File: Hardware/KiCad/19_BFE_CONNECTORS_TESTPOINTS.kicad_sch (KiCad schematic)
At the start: 0 parts

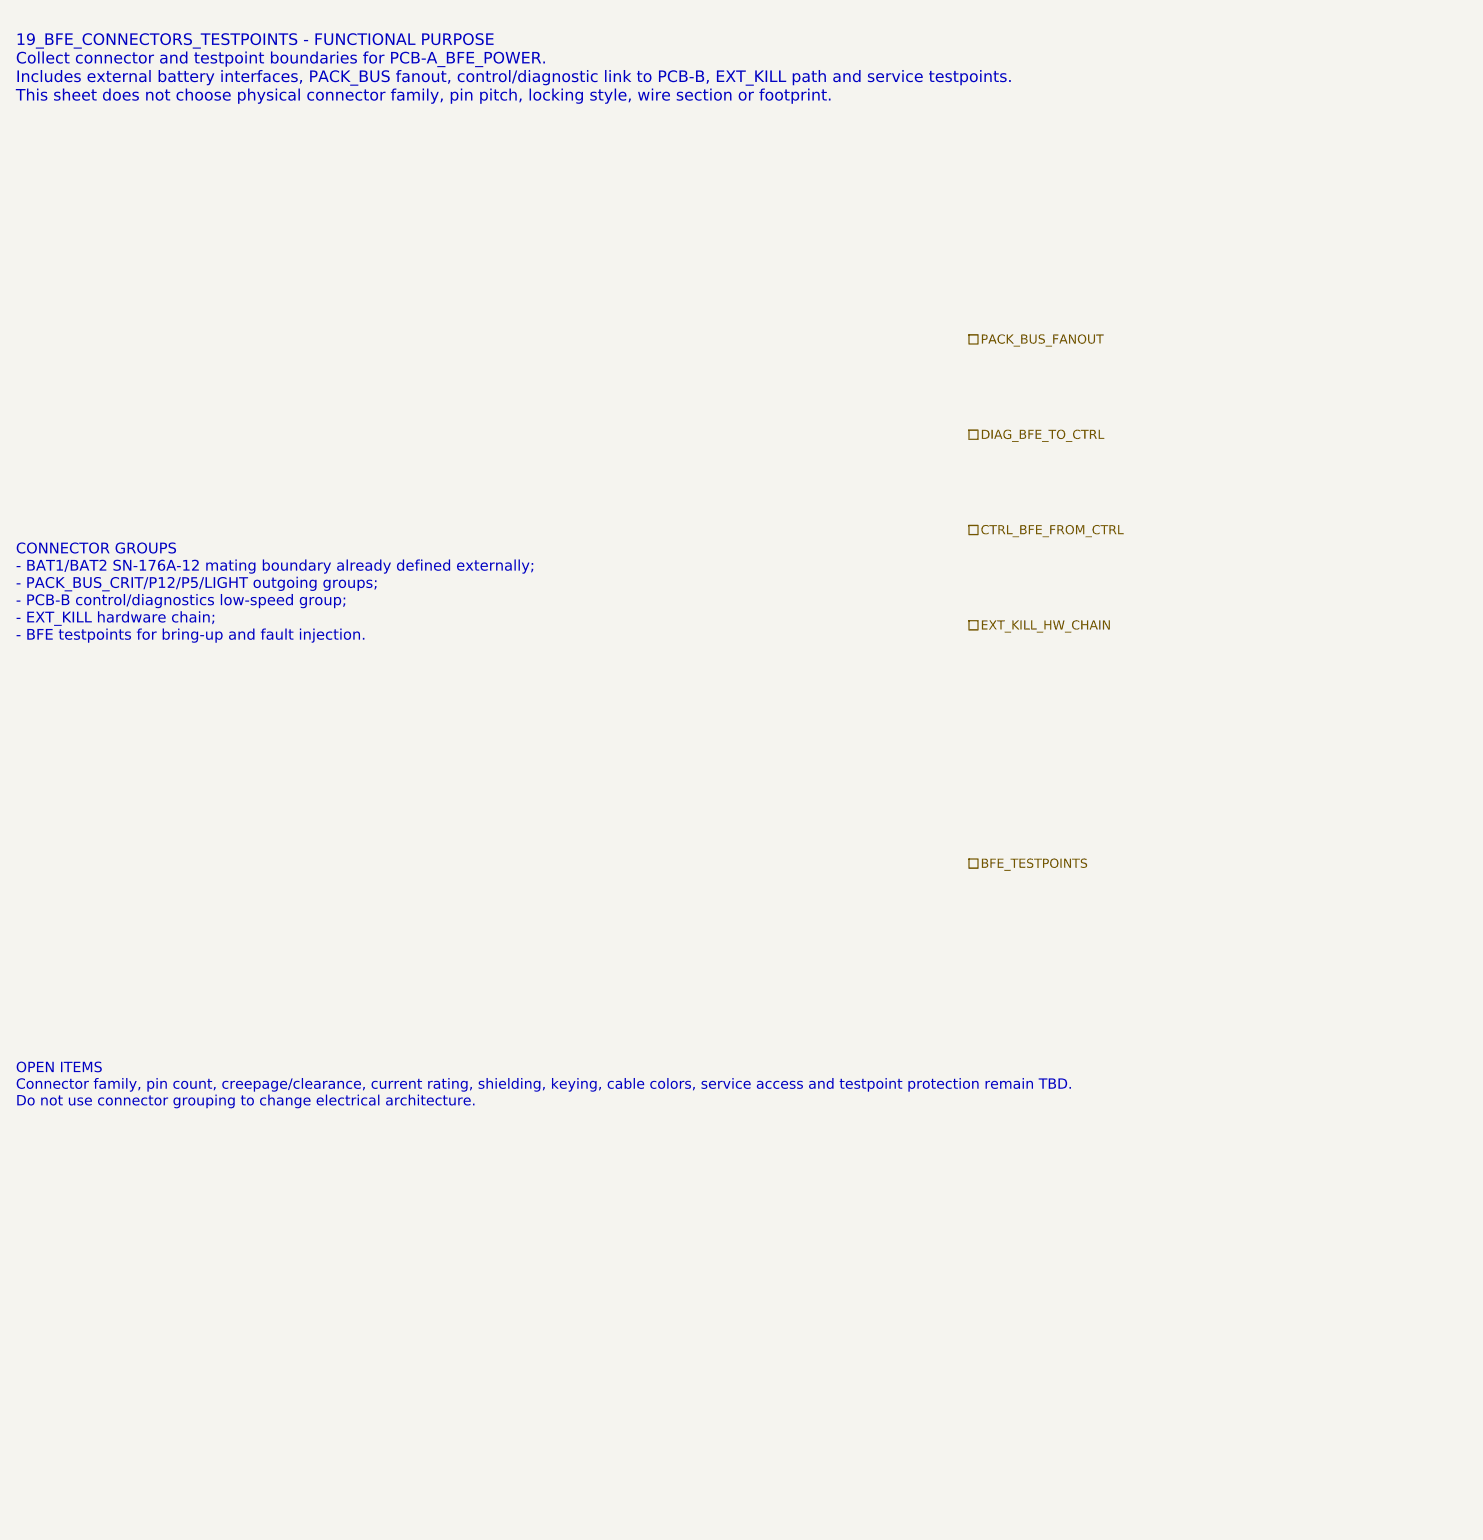
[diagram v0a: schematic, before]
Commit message: hardware: refine BFE connectors and testpoints level B
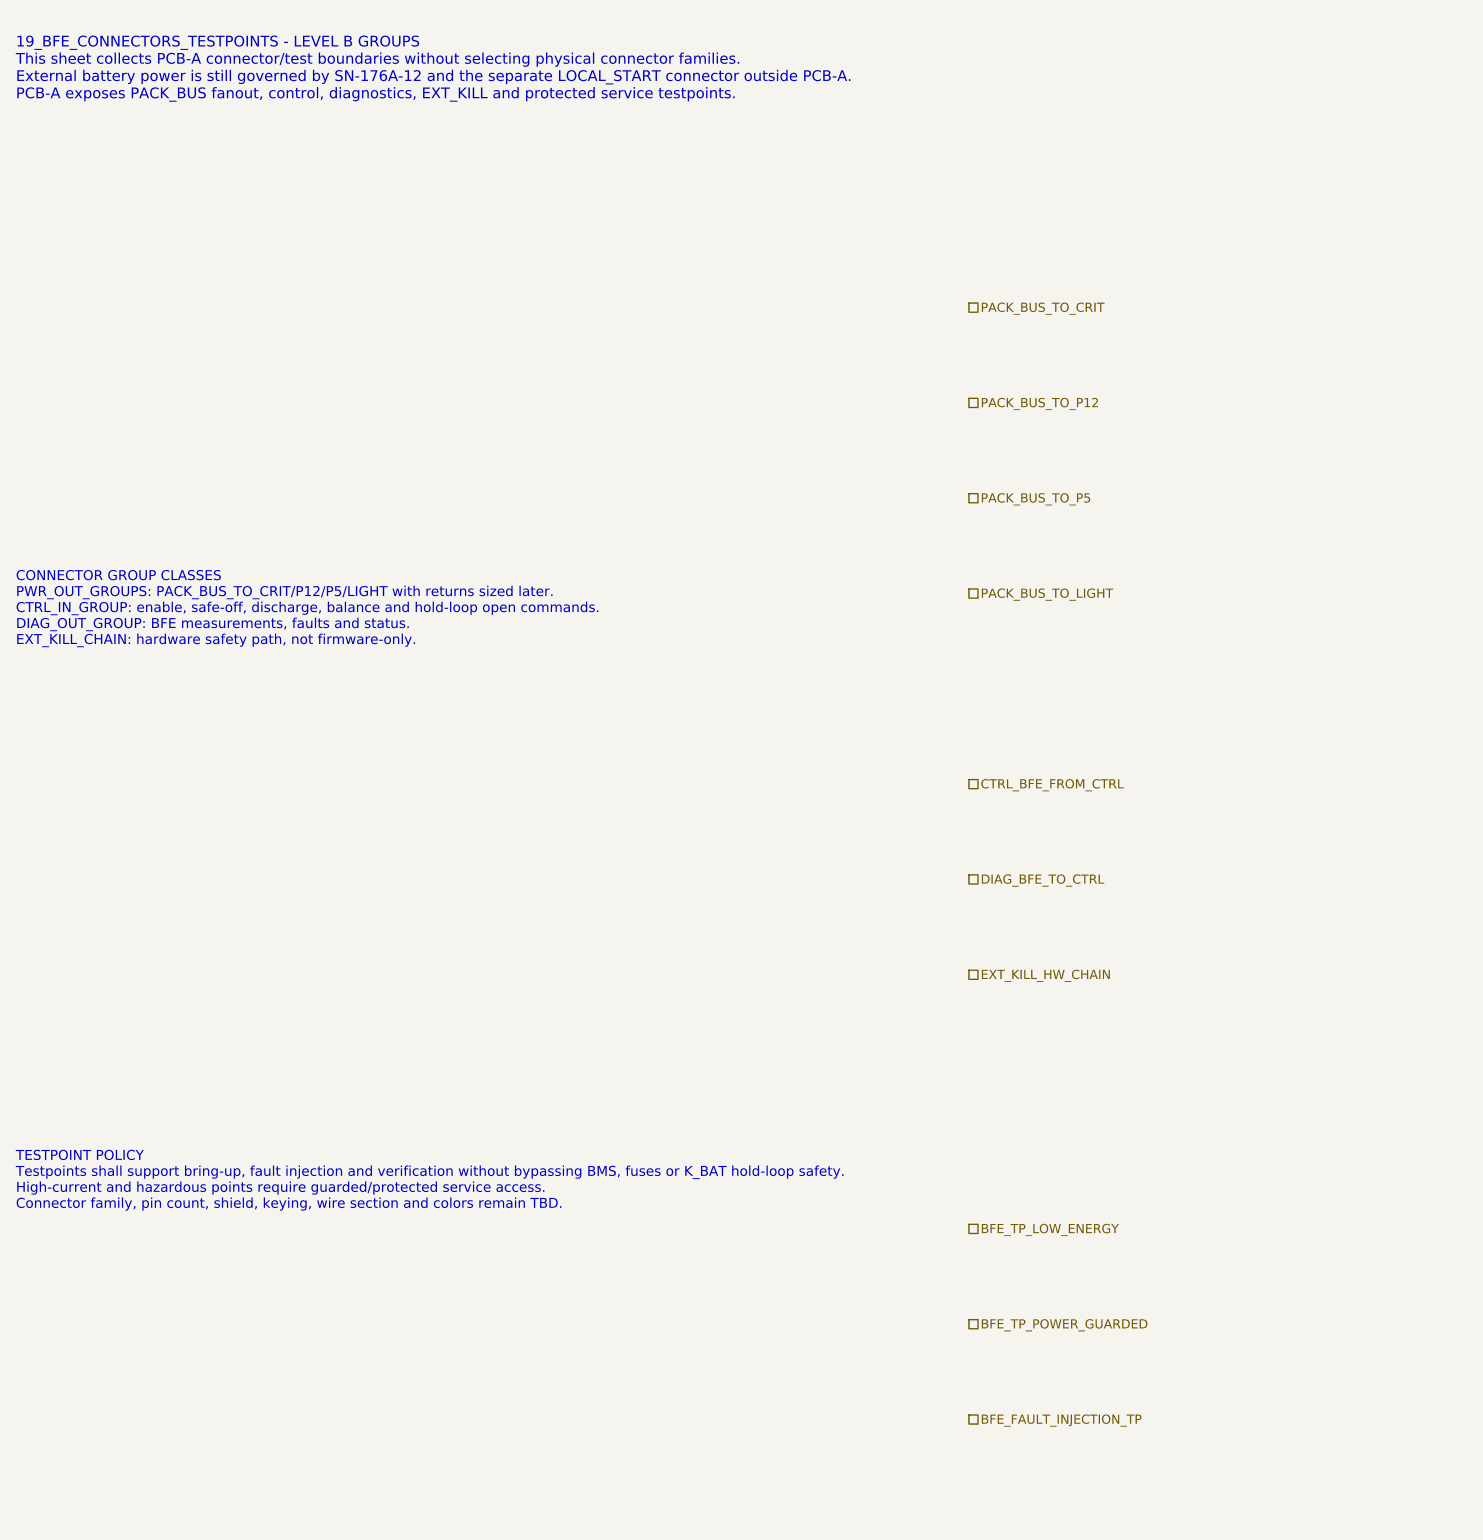
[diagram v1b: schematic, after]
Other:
- note added: "19_BFE_CONNECTORS_TESTPOINTS - LEVEL B GROUPS This sheet collects PCB-A connector/test boundaries without selecting physical connector families. External battery power is still governed by SN-176A-12 and the separate LOCAL_START connector outside PCB-A. PCB-A exposes PACK_BUS fanout, control, diagnostics, EXT_KILL and protected service testpoints."
- note added: "CONNECTOR GROUP CLASSES PWR_OUT_GROUPS: PACK_BUS_TO_CRIT/P12/P5/LIGHT with returns sized later. CTRL_IN_GROUP: enable, safe-off, discharge, balance and hold-loop open commands. DIAG_OUT_GROUP: BFE measurements, faults and status. EXT_KILL_CHAIN: hardware safety path, not firmware-only."
- note added: "TESTPOINT POLICY Testpoints shall support bring-up, fault injection and verification without bypassing BMS, fuses or K_BAT hold-loop safety. High-current and hazardous points require guarded/protected service access. Connector family, pin count, shield, keying, wire section and colors remain TBD."
- note removed: "19_BFE_CONNECTORS_TESTPOINTS - FUNCTIONAL PURPOSE Collect connector and testpoint boundaries for PCB-A_BFE_POWER. Includes external battery interfaces, PACK_BUS fanout, control/diagnostic link to PCB-B, EXT_KILL path and service testpoints. This sheet does not choose physical connector family, pin pitch, locking style, wire section or footprint."
- note removed: "CONNECTOR GROUPS - BAT1/BAT2 SN-176A-12 mating boundary already defined externally; - PACK_BUS_CRIT/P12/P5/LIGHT outgoing groups; - PCB-B control/diagnostics low-speed group; - EXT_KILL hardware chain; - BFE testpoints for bring-up and fault injection."
- note removed: "OPEN ITEMS Connector family, pin count, creepage/clearance, current rating, shielding, keying, cable colors, service access and testpoint protection remain TBD. Do not use connector grouping to change electrical architecture."
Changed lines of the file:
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@@
 	(generator "eeschema")
 	(generator_version "10.0")
-	(uuid "bfe-dh-00000019-0000-4000-8000-000000000019")
+	(uuid "bfe-lb-00000019-0000-4000-8000-000000000019")
 	(paper "A3")
 	(title_block
 		(title "19_BFE_CONNECTORS_TESTPOINTS - BFE connector/test boundary")
 		(date "2026-07-15")
-		(rev "A1")
+		(rev "B1")
 		(company "Gonoboben/plataVM")
-		(comment 1 "Architecture Level A: BFE external/internal connectors and testpoints")
-		(comment 2 "No physical connector families or footprints selected")
+		(comment 1 "Architecture Level B: connector groups and protected testpoint classes")
+		(comment 2 "No connector family, pin count, wire gauge or footprint selected")
 	)
-	(text "19_BFE_CONNECTORS_TESTPOINTS - FUNCTIONAL PURPOSE\nCollect connector and testpoint boundaries for PCB-A_BFE_POWER.\nIncludes external battery interfaces, PACK_BUS fanout, control/diagnostic link to PCB-B, EXT_KILL path and service testpoints.\nThis sheet does not choose physical connector family, pin pitch, locking style, wire section or footprint."
+	(text "19_BFE_CONNECTORS_TESTPOINTS - LEVEL B GROUPS\nThis sheet collects PCB-A connector/test boundaries without selecting physical connector families.\nExternal battery power is still governed by SN-176A-12 and the separate LOCAL_START connector outside PCB-A.\nPCB-A exposes PACK_BUS fanout, control, diagnostics, EXT_KILL and protected service testpoints."
 		(exclude_from_sim no)
 		(at 12 18 0)
-		(effects (font (size 1.45 1.45)) (justify left))
-		(uuid "bfe-dh-00000019-0000-4000-8000-000000000101")
+		(effects (font (size 1.35 1.35)) (justify left))
+		(uuid "bfe-lb-00000019-0000-4000-8000-000000000101")
 	)
-	(text "CONNECTOR GROUPS\n- BAT1/BAT2 SN-176A-12 mating boundary already defined externally;\n- PACK_BUS_CRIT/P12/P5/LIGHT outgoing groups;\n- PCB-B control/diagnostics low-speed group;\n- EXT_KILL hardware chain;\n- BFE testpoints for bring-up and fault injection."
+	(text "CONNECTOR GROUP CLASSES\nPWR_OUT_GROUPS: PACK_BUS_TO_CRIT/P12/P5/LIGHT with returns sized later.\nCTRL_IN_GROUP: enable, safe-off, discharge, balance and hold-loop open commands.\nDIAG_OUT_GROUP: BFE measurements, faults and status.\nEXT_KILL_CHAIN: hardware safety path, not firmware-only."
 		(exclude_from_sim no)
-		(at 12 84 0)
-		(effects (font (size 1.35 1.35)) (justify left))
-		(uuid "bfe-dh-00000019-0000-4000-8000-000000000102")
+		(at 12 86 0)
+		(effects (font (size 1.25 1.25)) (justify left))
+		(uuid "bfe-lb-00000019-0000-4000-8000-000000000102")
 	)
-	(text "OPEN ITEMS\nConnector family, pin count, creepage/clearance, current rating, shielding, keying, cable colors, service access and testpoint protection remain TBD.\nDo not use connector grouping to change electrical architecture."
+	(text "TESTPOINT POLICY\nTestpoints shall support bring-up, fault injection and verification without bypassing BMS, fuses or K_BAT hold-loop safety.\nHigh-current and hazardous points require guarded/protected service access.\nConnector family, pin count, shield, keying, wire section and colors remain TBD."
 		(exclude_from_sim no)
-		(at 12 146 0)
-		(effects (font (size 1.3 1.3)) (justify left))
-		(uuid "bfe-dh-00000019-0000-4000-8000-000000000103")
+		(at 12 158 0)
+		(effects (font (size 1.25 1.25)) (justify left))
+		(uuid "bfe-lb-00000019-0000-4000-8000-000000000103")
 	)
-	(hierarchical_label "PACK_BUS_FANOUT" (shape passive) (exclude_from_sim no) (at 132 52 0) (effects (font (size 1.15 1.15)) (justify left)) (uuid "bfe-dh-00000019-0000-4000-8000-000000000201"))
-	(hierarchical_label "DIAG_BFE_TO_CTRL" (shape passive) (exclude_from_sim no) (at 132 64 0) (effects (font (size 1.15 1.15)) (justify left)) (uuid "bfe-dh-00000019-0000-4000-8000-000000000202"))
-	(hierarchical_label "CTRL_BFE_FROM_CTRL" (shape passive) (exclude_from_sim no) (at 132 76 0) (effects (font (size 1.15 1.15)) (justify left)) (uuid "bfe-dh-00000019-0000-4000-8000-000000000203"))
-	(hierarchical_label "EXT_KILL_HW_CHAIN" (shape passive) (exclude_from_sim no) (at 132 88 0) (effects (font (size 1.15 1.15)) (justify left)) (uuid "bfe-dh-00000019-0000-4000-8000-000000000204"))
-	(hierarchical_label "BFE_TESTPOINTS" (shape passive) (exclude_from_sim no) (at 132 118 0) (effects (font (size 1.15 1.15)) (justify left)) (uuid "bfe-dh-00000019-0000-4000-8000-000000000205"))
+	(hierarchical_label "PACK_BUS_TO_CRIT" (shape passive) (exclude_from_sim no) (at 132 48 0) (effects (font (size 1.15 1.15)) (justify left)) (uuid "bfe-lb-00000019-0000-4000-8000-000000000201"))
+	(hierarchical_label "PACK_BUS_TO_P12" (shape passive) (exclude_from_sim no) (at 132 60 0) (effects (font (size 1.15 1.15)) (justify left)) (uuid "bfe-lb-00000019-0000-4000-8000-000000000202"))
+	(hierarchical_label "PACK_BUS_TO_P5" (shape passive) (exclude_from_sim no) (at 132 72 0) (effects (font (size 1.15 1.15)) (justify left)) (uuid "bfe-lb-00000019-0000-4000-8000-000000000203"))
+	(hierarchical_label "PACK_BUS_TO_LIGHT" (shape passive) (exclude_from_sim no) (at 132 84 0) (effects (font (size 1.15 1.15)) (justify left)) (uuid "bfe-lb-00000019-0000-4000-8000-000000000204"))
+	(hierarchical_label "CTRL_BFE_FROM_CTRL" (shape passive) (exclude_from_sim no) (at 132 108 0) (effects (font (size 1.15 1.15)) (justify left)) (uuid "bfe-lb-00000019-0000-4000-8000-000000000205"))
+	(hierarchical_label "DIAG_BFE_TO_CTRL" (shape passive) (exclude_from_sim no) (at 132 120 0) (effects (font (size 1.15 1.15)) (justify left)) (uuid "bfe-lb-00000019-0000-4000-8000-000000000206"))
+	(hierarchical_label "EXT_KILL_HW_CHAIN" (shape passive) (exclude_from_sim no) (at 132 132 0) (effects (font (size 1.15 1.15)) (justify left)) (uuid "bfe-lb-00000019-0000-4000-8000-000000000207"))
+	(hierarchical_label "BFE_TP_LOW_ENERGY" (shape passive) (exclude_from_sim no) (at 132 164 0) (effects (font (size 1.15 1.15)) (justify left)) (uuid "bfe-lb-00000019-0000-4000-8000-000000000208"))
+	(hierarchical_label "BFE_TP_POWER_GUARDED" (shape passive) (exclude_from_sim no) (at 132 176 0) (effects (font (size 1.15 1.15)) (justify left)) (uuid "bfe-lb-00000019-0000-4000-8000-000000000209"))
+	(hierarchical_label "BFE_FAULT_INJECTION_TP" (shape passive) (exclude_from_sim no) (at 132 188 0) (effects (font (size 1.15 1.15)) (justify left)) (uuid "bfe-lb-00000019-0000-4000-8000-000000000210"))
 )
